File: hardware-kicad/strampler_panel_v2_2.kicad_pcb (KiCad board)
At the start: 2 copper layers, 91.3 x 128.5 mm, 32 parts

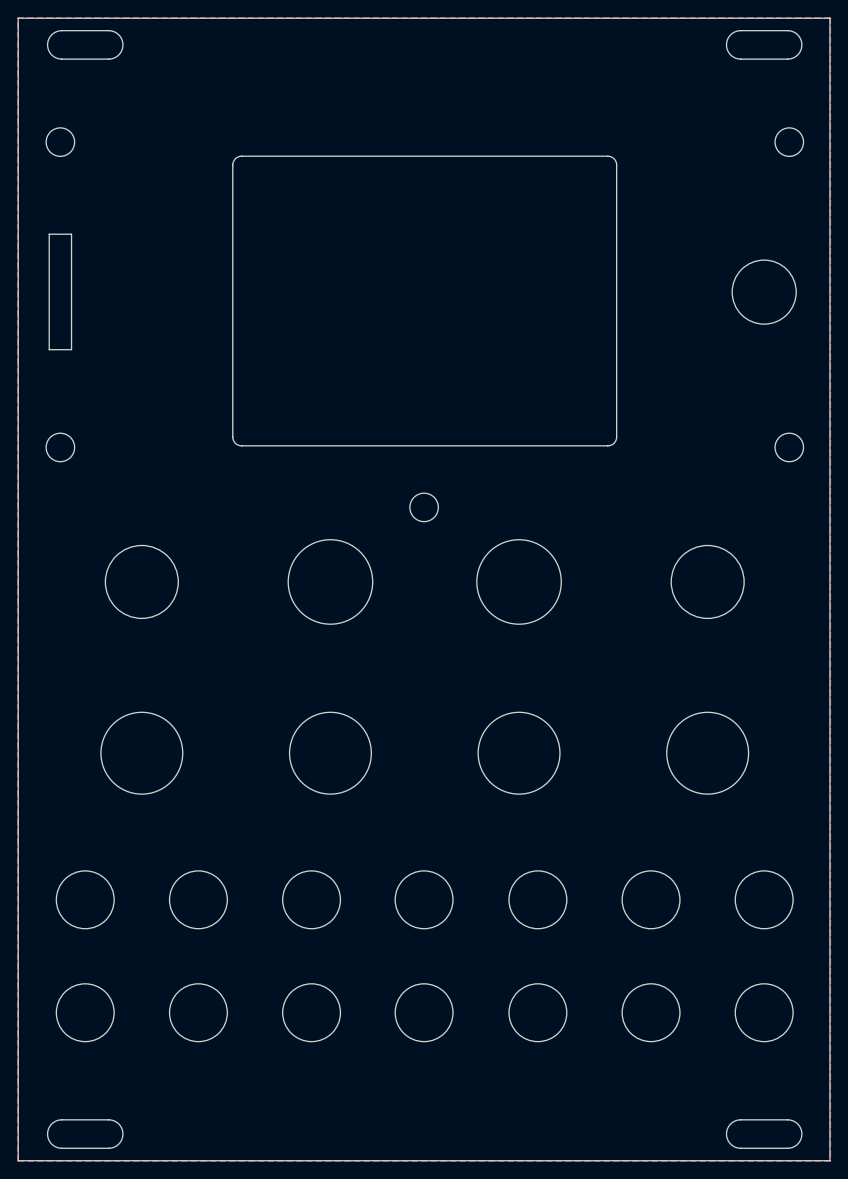
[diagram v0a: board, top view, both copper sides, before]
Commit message: Fix panel gerbers: fill copper pours, convert art zones to filled shapes
PCBWay's audit caught empty copper: the Eagle importer produces UNFILLED
zones, which plot as nothing — copper pours, mask openings AND the 34k-rect
silkscreen artwork were all missing from the first plot. Copper zones are
now filled (pcbnew ZONE_FILLER) and all non-copper zones converted to
filled gr_poly shapes via the pcbnew API. Panel .kicad_pcb updated to the
fixed board; gerber zip regenerated (front silk now 4.4 MB of art).

Co-Authored-By: Claude Fable 5 <noreply@anthropic.com>
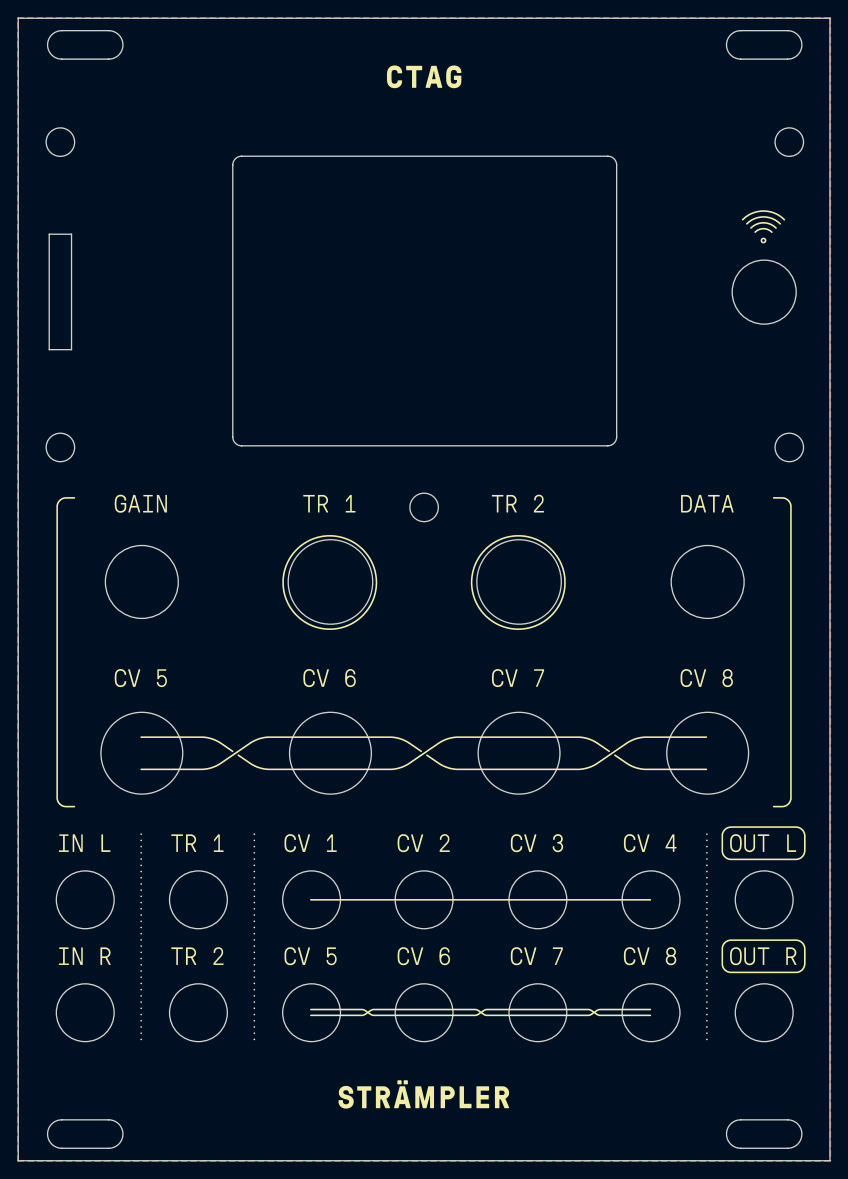
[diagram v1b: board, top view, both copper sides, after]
